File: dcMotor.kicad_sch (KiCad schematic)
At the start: 124 parts, among them J1 USB_C_Receptacle_USB2.0_16P, J2 USB_C_Receptacle_USB2.0_16P, J3 Conn_ST_STDC14, J6 Conn_01x02_Pin, J7 Conn_01x04_Pin, J8 Conn_01x06_Pin, Q1 AO3400A, SW1 SW_Push, SW2 SW_Push, U1 LMR54406DBVR, U10 MCP6561-OT, U12 NUCLEO-F411RE, U2 NCP718ASNADJT1G, U3 NCP718ASNADJT1G, U5 TLV9152IDR, U6 ER_OLEDM0.91_1x-I2C, U7 STM32G431CBTx, U8 LTH-301-05, U9 DRV8231ADDA

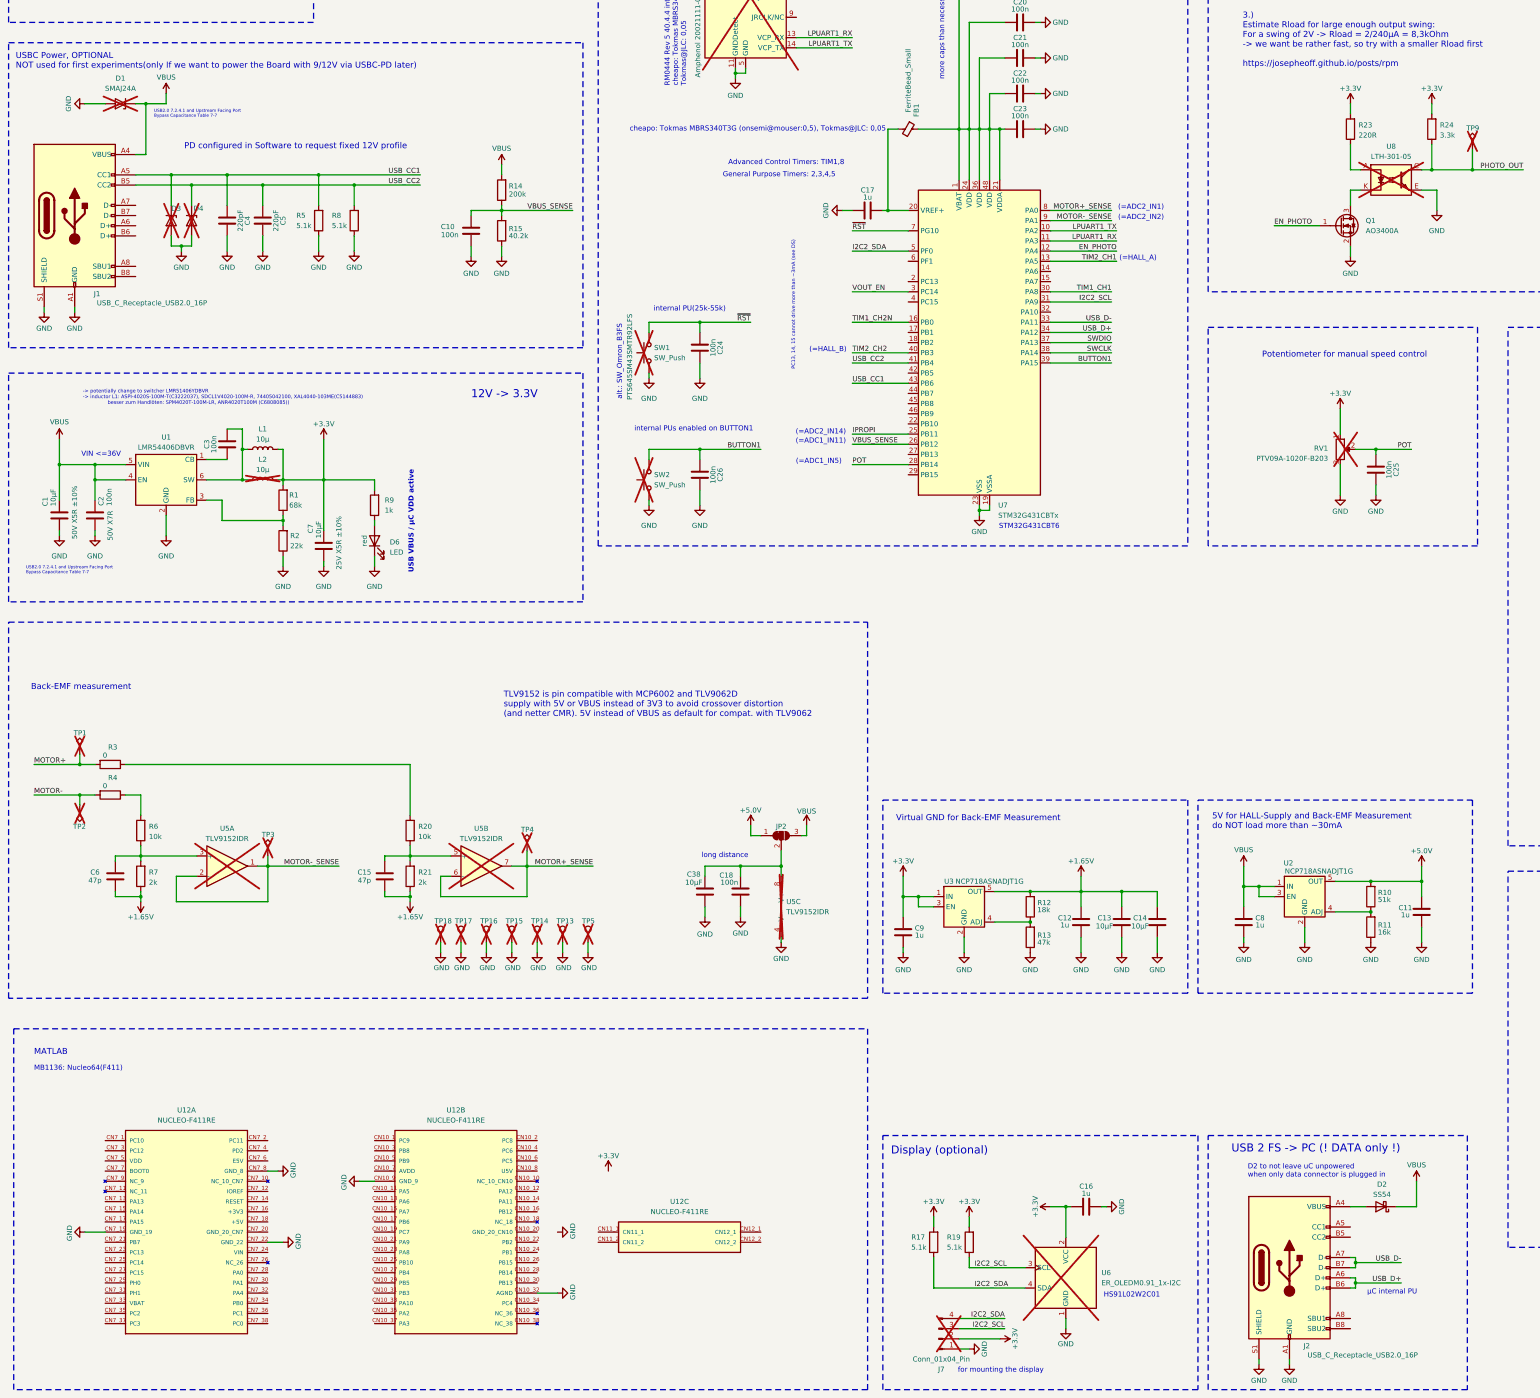
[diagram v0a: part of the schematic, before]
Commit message: remove 2nd USB connector
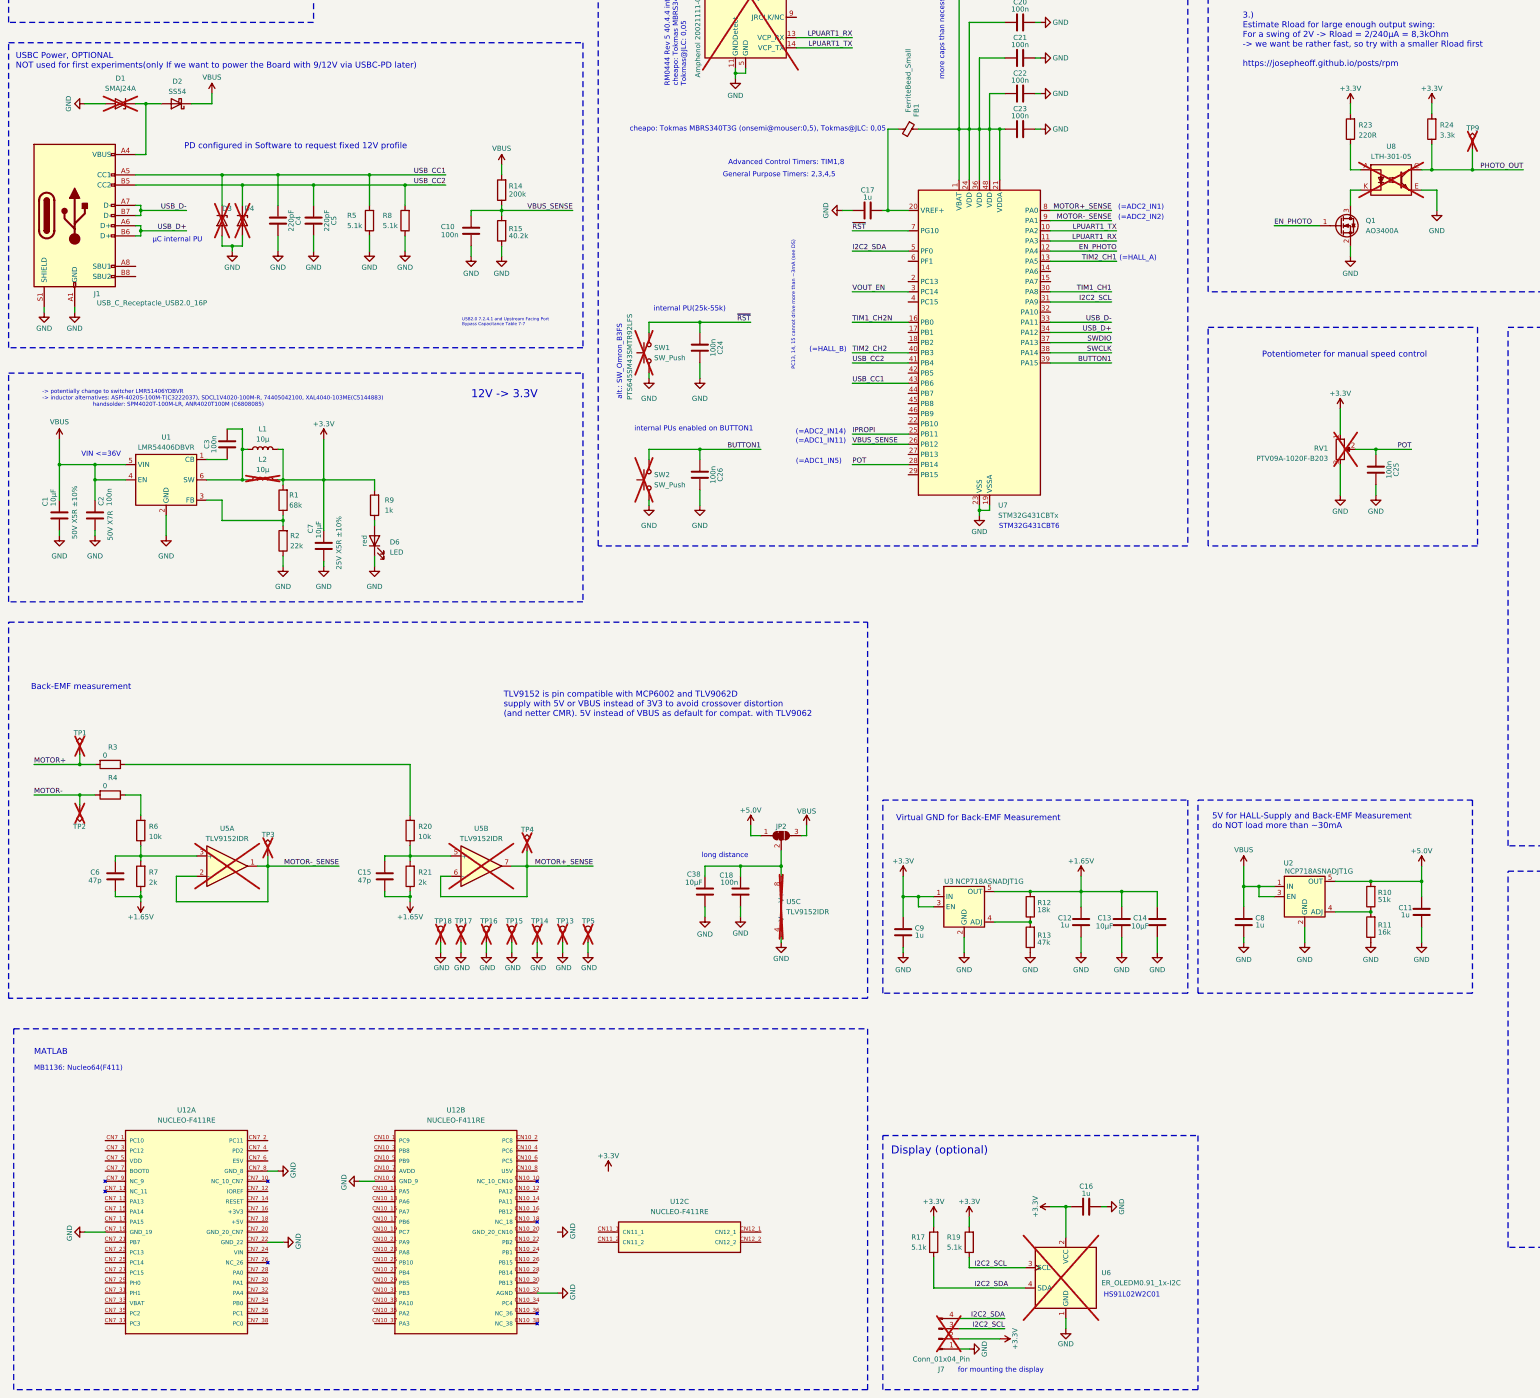
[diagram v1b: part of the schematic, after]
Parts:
- removed J2: USB_C_Receptacle_USB2.0_16P, Connector_USB:USB_C_Receptacle_HCTL_HC-TYPE-C-16P-01A, symbol Connector:USB_C_Receptacle_USB2.0_16P
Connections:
- net USB_D+: now also J1.A6 (D+), J1.B6 (D+)
- net USB_D-: now also J1.A7 (D-), J1.B7 (D-)
- net VBUS: no longer D1.1 (A1), J1.A4 (VBUS), J1.A9 (VBUS), J1.B4 (VBUS), J1.B9 (VBUS)
- net at D2.2 (A): now also D1.1 (A1), J1.A4 (VBUS), J1.A9 (VBUS), J1.B4 (VBUS), J1.B9 (VBUS)
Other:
- note added: "-> potentially change to switcher LMR51406YDBVR -> inductor alternatives: ASPI-4020S-100M-T(C3222037), SDCL1V4020-100M-R, 74405042100, XAL4040-103ME(C5144883) handsolder: SPM4020T-100M-LR, ANR4020T100M (C6808085)"
- note removed: "-> potentially change to switcher LMR51406YDBVR -> inductor L1: ASPI-4020S-100M-T(C3222037), SDCL1V4020-100M-R, 74405042100, XAL4040-103ME(C5144883) besser zum Handlöten: SPM4020T-100M-LR, ANR4020T100M (C6808085))"
- note removed: "D2 to not leave uC unpowered when only data connector is plugged in"
- note removed: "USB 2 FS -> PC (! DATA only !)"
- note removed: "USB VBUS / µC VDD active"
- moved on the sheet: C4, C5, D2, D3, D4, R5, R8

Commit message: applied 2nd USB connector removal to layout
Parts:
- U12: value NUCLEO-F411RE -> NUCLEO-F411RE:NUCLEO-F411RE
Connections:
- net GND: now also J6.1 (Pin_1); no longer J6.2 (Pin_2)
- net VBUS: no longer R14.2
- net at D5.2 (A): now also J6.2 (Pin_2); no longer J6.1 (Pin_1)
- net at D1.1 (A1), D2.2 (A), J1.A4 (VBUS)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: now also R14.2
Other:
- note added: "USB Data onboard µC<->PC. USBC Power OPTIONAL NOT used for first experiments only If we want to power the Board with 9/12V via USBC-PD later (not sure if usbcpd negotiation hsa trouble with D2/D5)"
- note added: "dummy symbol to include motor mechanical step"
- note removed: "USBC Power, OPTIONAL NOT used for first experiments(only If we want to power the Board with 9/12V via USBC-PD later)"
- moved on the sheet: C10, R14, R15

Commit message: latest rev for review
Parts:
- added H1: MountingHole, symbol Mechanical:MountingHole
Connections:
- net BUTTON1: now also U12.CN10_37 (PA3)
- net EN_PHOTO: now also U12.CN10_35 (PA2)
- net I2C2_SCL: now also U12.CN10_25 (PB10)
- net I2C2_SDA: now also U12.CN10_31 (PB3)
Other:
- note added: "(=MOTOR_DRV_IN1)"
- note added: "(=MOTOR_DRV_IN2)"
- note added: "CN10"
- note added: "CN7"
- moved on the sheet: C11, C12, C13, C14, C16, C8, C9, J7, R10, R11, R12, R13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

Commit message: connect nucleo
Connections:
- net BUTTON1: now also U12.CN10_29 (PB5); no longer U12.CN10_37 (PA3)
- net EN_PHOTO: now also U12.CN10_27 (PB4); no longer U12.CN10_35 (PA2)
- net IPROPI: now also U12.CN7_36 (PC1)
- net MOTOR+_SENSE: now also U12.CN10_35 (PA2)
- net MOTOR-_SENSE: now also U12.CN10_37 (PA3)
- net POT: now also U12.CN7_38 (PC0)
- net TIM1_CH1: now also U12.CN7_28 (PA0)
- net TIM1_CH2N: now also U12.CN7_30 (PA1)
- net TIM2_CH1: now also U12.CN7_34 (PB0)
- net TIM2_CH2: now also U12.CN7_32 (PA4)
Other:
- moved on the sheet: U12A, U12B, U12C

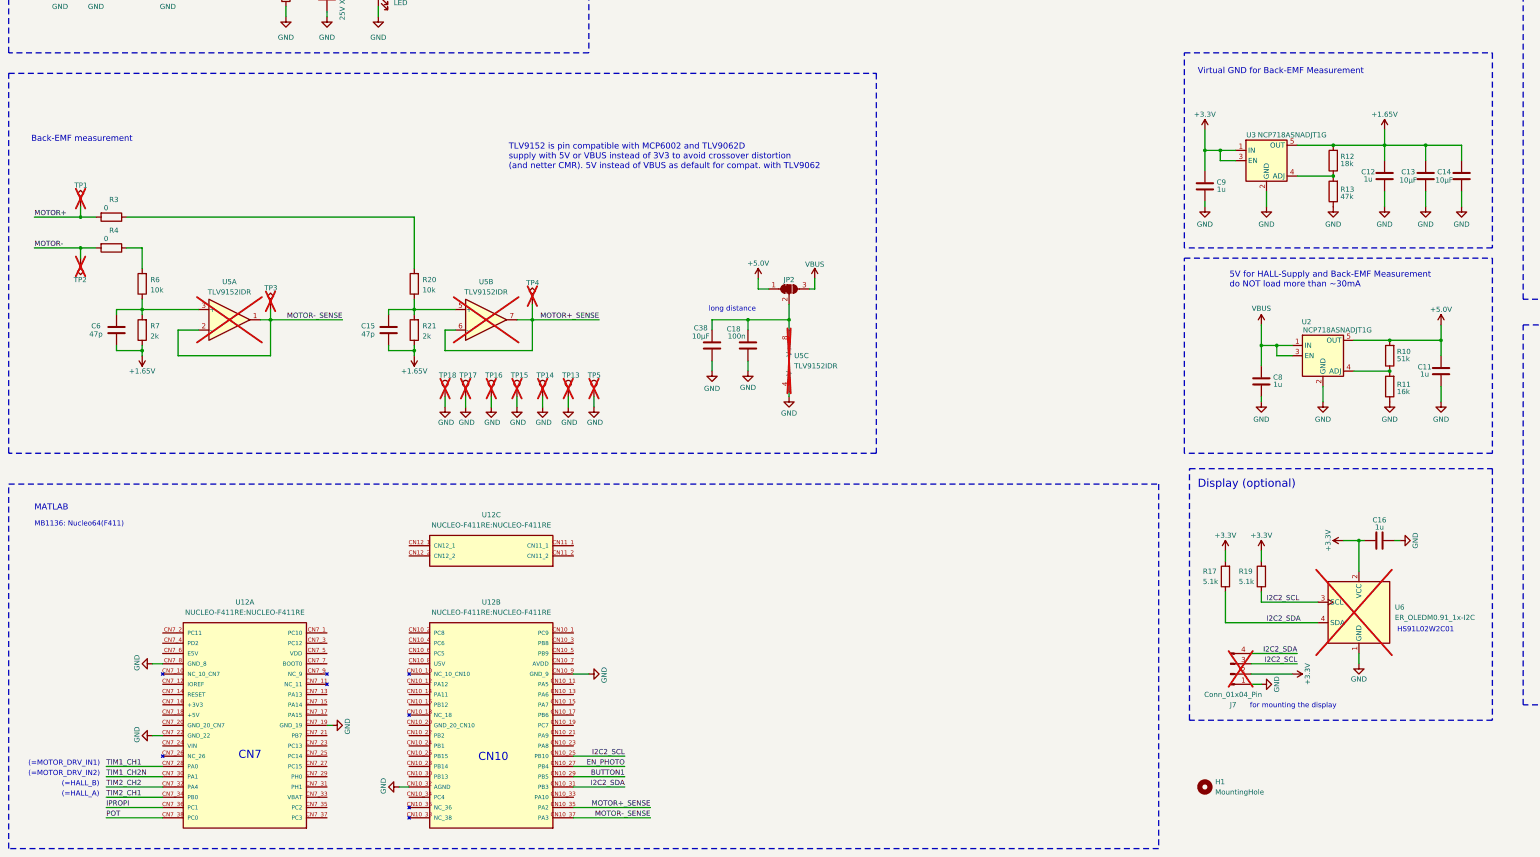
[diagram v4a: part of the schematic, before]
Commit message: added diffamp just for experimenting
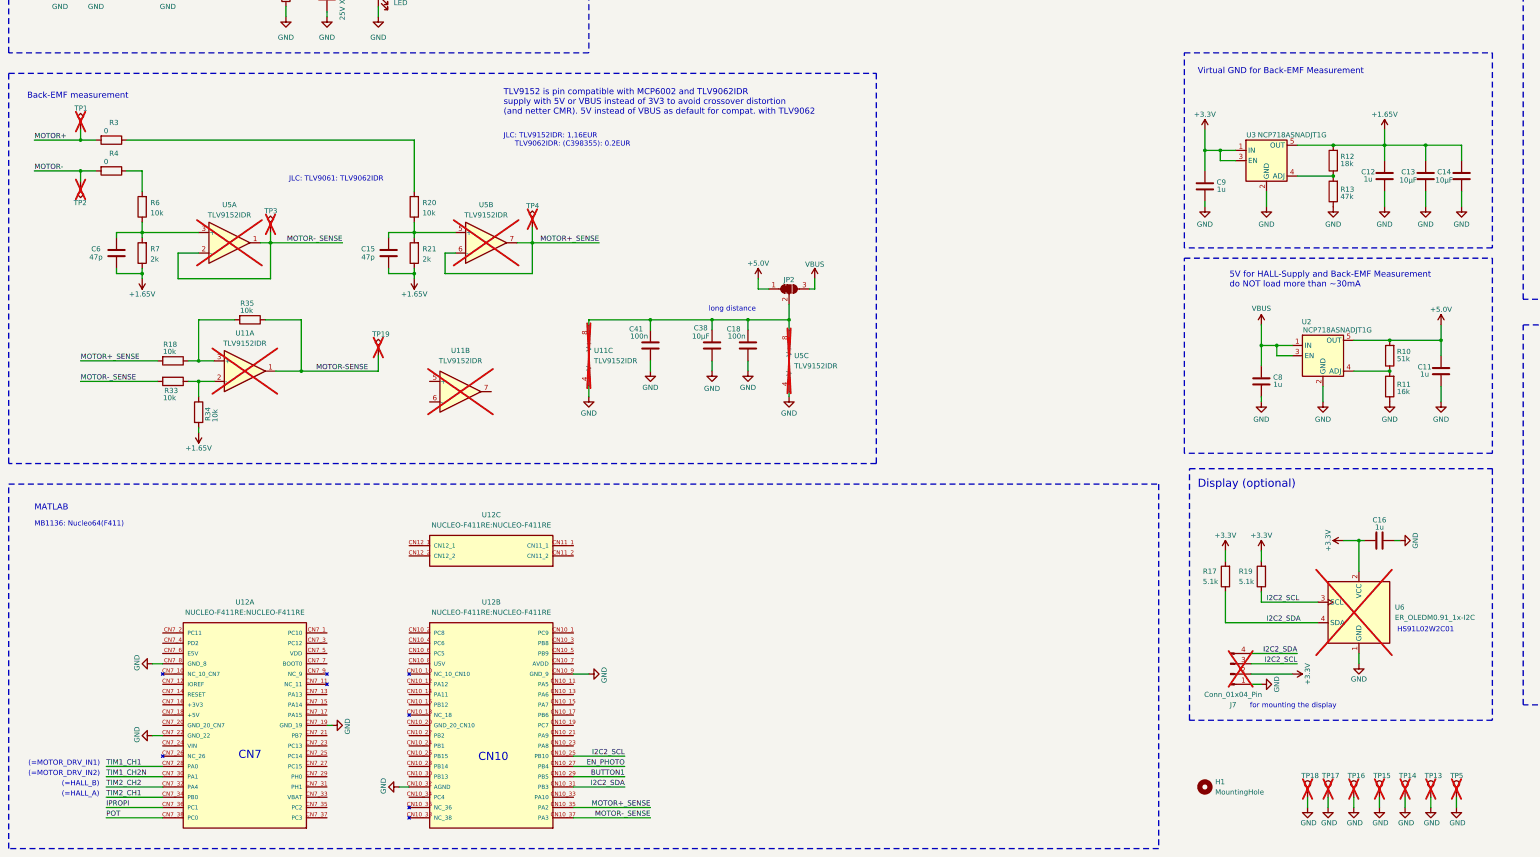
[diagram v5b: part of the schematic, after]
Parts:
- added C41: 100n, Capacitor_SMD:C_0402_1005Metric, symbol Device:C
- added R18, R33, R34, R35: 10k, Resistor_SMD:R_0805_2012Metric, symbol Device:R
- added TP19: TP_Keystone_5095, PZ:TP_Keystone_5010-5014_Multipurpose, symbol PZ:TP_Keystone_5010-5014_Multipurpose
- added U11: TLV9152IDR, Package_SO:SOIC-8_3.9x4.9mm_P1.27mm, symbol PZ:TLV9152IDR
- U5: LCSC Part # C882649 -> C398355
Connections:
- net +1.65V: now also R34.2
- net GND: now also C41.1, U11.4 (V-)
- net MOTOR+_SENSE: now also R18.2
- net MOTOR-_SENSE: now also R33.2
- net at C18.2, C38.2, JP2.2 (C)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: now also C41.2, U11.8 (V+)
- new net: R33.1, R34.1, U11.2 (-)
- new net: R18.1, R35.2, U11.3 (+)
- new net MOTOR-SENSE: R35.1, TP19.1, U11.1
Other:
- note added: "JLC: TLV9061: TLV9062IDR"
- note added: "JLC: TLV9152IDR: 1,16EUR TLV9062IDR: (C398355): 0.2EUR"
- note added: "TLV9152 is pin compatible with MCP6002 and TLV9062IDR supply with 5V or VBUS instead of 3V3 to avoid crossover distortion (and netter CMR). 5V instead of VBUS as default for compat. with TLV9062"
- note removed: "TLV9152 is pin compatible with MCP6002 and TLV9062D supply with 5V or VBUS instead of 3V3 to avoid crossover distortion (and netter CMR). 5V instead of VBUS as default for compat. with TLV9062"
- moved on the sheet: C15, C6, R20, R21, R3, R4, R6, R7, TP1, TP13, TP14, TP15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

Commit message: ioc cube file for 32pin nucleo fpr quick PWM test
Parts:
- added R36: 0, Resistor_SMD:R_0805_2012Metric, symbol Device:R
- added unit 3 of U11
- added unit 1 of U11
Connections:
- net BUTTON1: now also U7.42 (PB5); no longer U7.39 (PA15)
- net GND: now also R36.1, U11.4 (V-); no longer U11.4 (V-)
- net MOTOR-SENSE: now also U11.1; no longer U11.1
- net at R33.1, R34.1: now also U11.2 (-); no longer U11.2 (-)
- net at R18.1, R35.2: now also U11.3 (+); no longer U11.3 (+)
- net at C18.2, C38.2, C41.2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: now also U11.8 (V+); no longer U11.8 (V+)
- net I2C1_SDA: now reaches U7.44 (PB7)
- net I2C1_SDA: now also J7.4 (Pin_4), R17.1, U6.4 (SDA)
- net at Q1.3 (D), U8.K: now also R36.2
- net I2C2_SCL renamed I2C1_SCL
- net I2C1_SCL: now also U7.39 (PA15); no longer U12.CN10_25 (PB10), U7.31 (PA9)
- removed net I2C2_SDA: J7.4 (Pin_4), R17.1, U12.CN10_31 (PB3), U6.4 (SDA), U7.5 (PF0)
- net TIM1_CH2N renamed TIM1_CH2
- net TIM1_CH2: now also U7.31 (PA9); no longer U7.16 (PB0)
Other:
- moved on the sheet: Q1
